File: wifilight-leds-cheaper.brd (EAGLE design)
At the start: 50.8 x 50.8 mm, 37 parts, among them Q1 BUK98180-100A, Q2 BUK98180-100A, Q3 BUK98180-100A, Q4 BUK98180-100A, U2 PCA9685

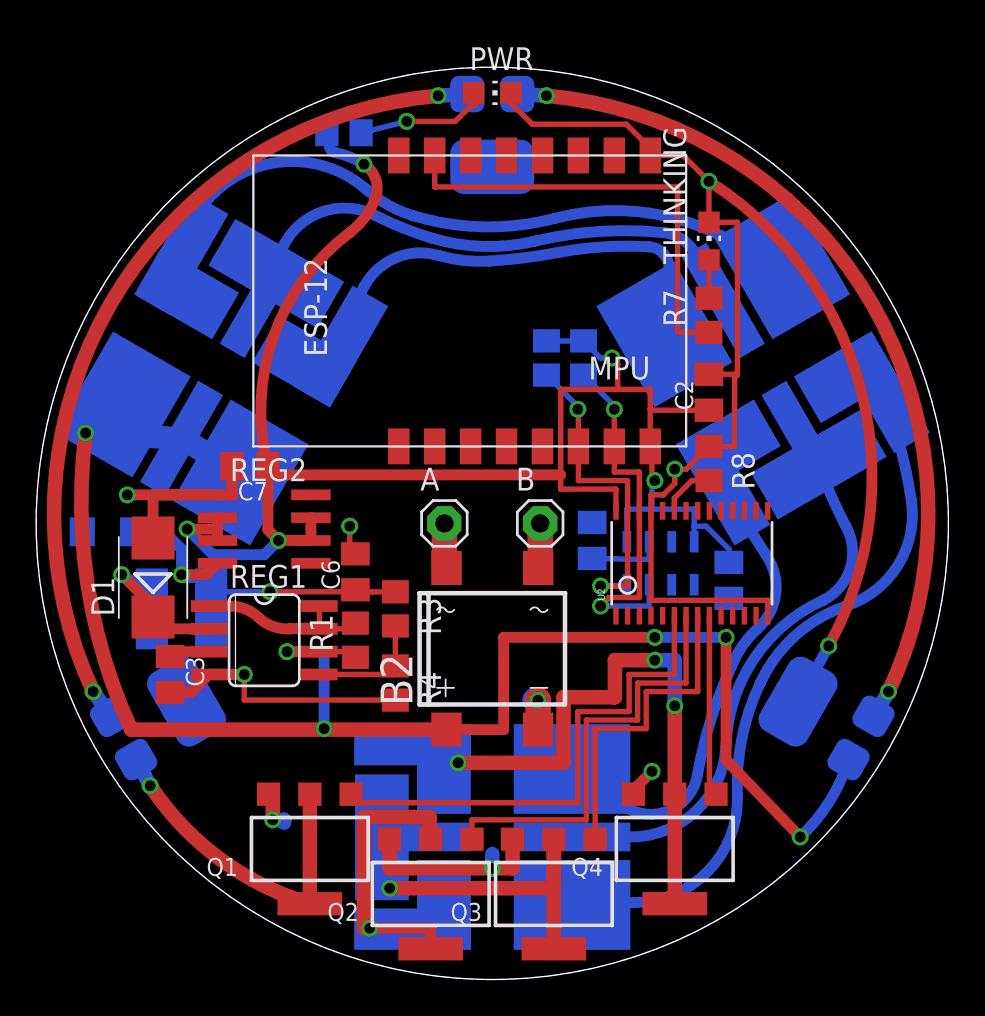
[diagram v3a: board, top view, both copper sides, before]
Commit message: Add a second ground plane on the top surface, pump it full of vias to help add thermal mass and heat spreading
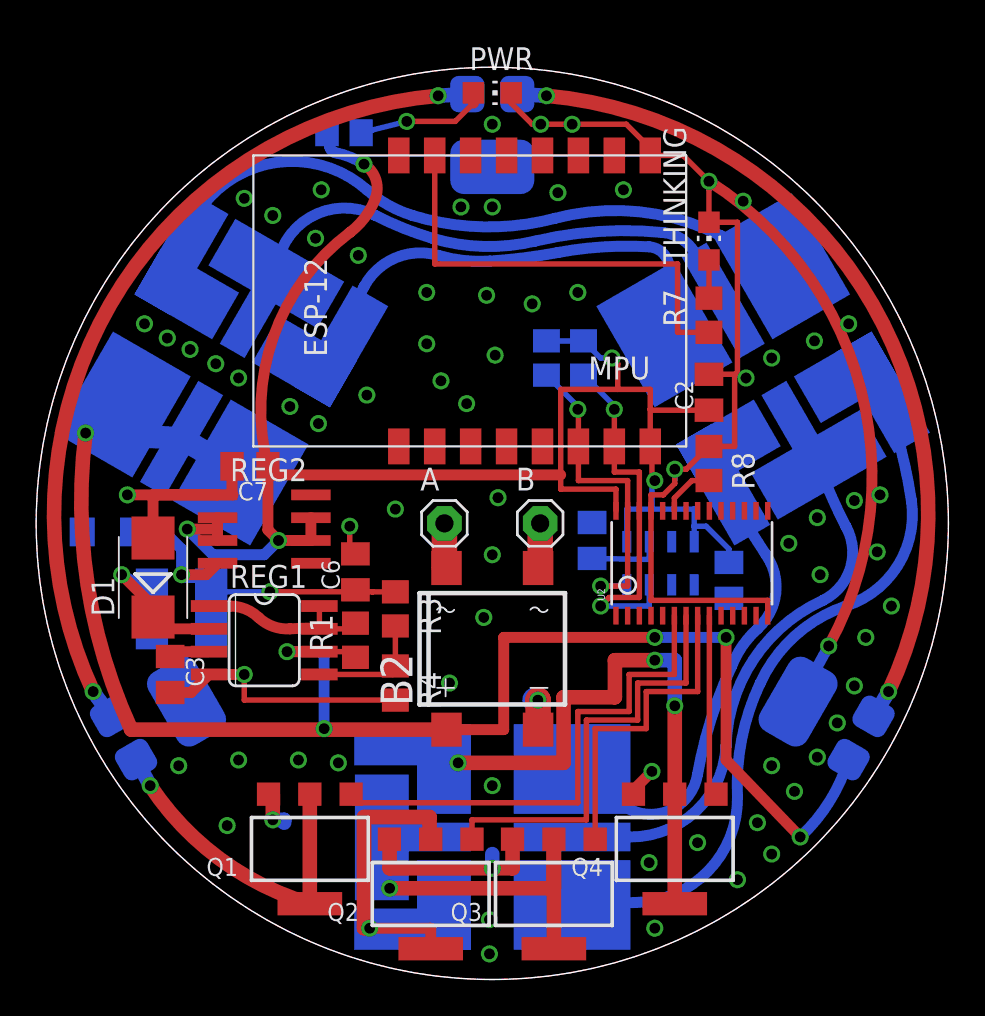
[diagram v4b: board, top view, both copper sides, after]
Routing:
- net GND: vias 10 -> 75
- added copper zone on layer 1, net GND
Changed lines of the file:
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@@
 <wire x1="26.45" y1="49.37125" x2="26.45" y2="48.7975" width="0.3048" layer="1"/>
 <wire x1="26.45" y1="48.7975" x2="27.6225" y2="47.625" width="0.3048" layer="1"/>
-<wire x1="27.6225" y1="47.625" x2="32.86125" y2="47.625" width="0.3048" layer="1"/>
+<wire x1="27.6225" y1="47.625" x2="28.09875" y2="47.625" width="0.3048" layer="1"/>
+<wire x1="28.09875" y1="47.625" x2="29.845" y2="47.625" width="0.3048" layer="1"/>
+<wire x1="29.845" y1="47.625" x2="32.86125" y2="47.625" width="0.3048" layer="1"/>
 <wire x1="32.86125" y1="47.625" x2="33.9725" y2="46.51375" width="0.3048" layer="1"/>
 <wire x1="33.9725" y1="46.51375" x2="33.9725" y2="46.10875" width="0.3048" layer="1"/>
@@
 <wire x1="34.29" y1="11.58875" x2="33.26" y2="10.55875" width="0.6096" layer="1"/>
 <wire x1="33.26" y1="10.55875" x2="33.26" y2="10.32075" width="0.6096" layer="1"/>
+<polygon width="0.6096" layer="1">
+<vertex x="25.4" y="50.8" curve="90"/>
+<vertex x="0" y="25.4" curve="90"/>
+<vertex x="25.4" y="0" curve="90"/>
+<vertex x="50.8" y="25.4" curve="90"/>
+</polygon>
+<via x="28.09875" y="47.625" extent="1-16" drill="0.6"/>
+<via x="29.845" y="47.625" extent="1-16" drill="0.6"/>
+<via x="17.93875" y="40.3225" extent="1-16" drill="0.6"/>
+<via x="21.74875" y="38.25875" extent="1-16" drill="0.6"/>
+<via x="21.74875" y="35.40125" extent="1-16" drill="0.6"/>
+<via x="22.5425" y="33.3375" extent="1-16" drill="0.6"/>
+<via x="23.97125" y="32.0675" extent="1-16" drill="0.6"/>
+<via x="25.55875" y="34.76625" extent="1-16" drill="0.6"/>
+<via x="25.0825" y="38.1" extent="1-16" drill="0.6"/>
+<via x="27.6225" y="37.62375" extent="1-16" drill="0.6"/>
+<via x="30.1625" y="38.25875" extent="1-16" drill="0.6"/>
+<via x="25.4" y="47.625" extent="1-16" drill="0.6"/>
+<via x="18.415" y="32.54375" extent="1-16" drill="0.6"/>
+<via x="7.9375" y="11.90625" extent="1-16" drill="0.6"/>
+<via x="11.27125" y="12.22375" extent="1-16" drill="0.6"/>
+<via x="10.63625" y="8.5725" extent="1-16" drill="0.6"/>
+<via x="14.605" y="12.22375" extent="1-16" drill="0.6"/>
+<via x="16.8275" y="12.065" extent="1-16" drill="0.6"/>
+<via x="25.24125" y="3.33375" extent="1-16" drill="0.6"/>
+<via x="25.24125" y="1.42875" extent="1-16" drill="0.6"/>
+<via x="42.2275" y="10.4775" extent="1-16" drill="0.6"/>
+<via x="40.9575" y="11.90625" extent="1-16" drill="0.6"/>
+<via x="43.4975" y="12.3825" extent="1-16" drill="0.6"/>
+<via x="44.60875" y="14.2875" extent="1-16" drill="0.6"/>
+<via x="45.56125" y="16.35125" extent="1-16" drill="0.6"/>
+<via x="46.19625" y="19.05" extent="1-16" drill="0.6"/>
+<via x="47.625" y="20.79625" extent="1-16" drill="0.6"/>
+<via x="43.65625" y="22.5425" extent="1-16" drill="0.6"/>
+<via x="43.4975" y="25.7175" extent="1-16" drill="0.6"/>
+<via x="41.91" y="24.28875" extent="1-16" drill="0.6"/>
+<via x="45.56125" y="26.67" extent="1-16" drill="0.6"/>
+<via x="46.99" y="26.9875" extent="1-16" drill="0.6"/>
+<via x="46.83125" y="23.8125" extent="1-16" drill="0.6"/>
+<via x="39.52875" y="33.49625" extent="1-16" drill="0.6"/>
+<via x="40.9575" y="34.6075" extent="1-16" drill="0.6"/>
+<via x="43.33875" y="35.56" extent="1-16" drill="0.6"/>
+<via x="45.24375" y="36.5125" extent="1-16" drill="0.6"/>
+<via x="15.71625" y="30.95625" extent="1-16" drill="0.6"/>
+<via x="11.27125" y="33.49625" extent="1-16" drill="0.6"/>
+<via x="10.00125" y="34.29" extent="1-16" drill="0.6"/>
+<via x="8.5725" y="35.08375" extent="1-16" drill="0.6"/>
+<via x="7.3025" y="35.71875" extent="1-16" drill="0.6"/>
+<via x="6.0325" y="36.5125" extent="1-16" drill="0.6"/>
+<via x="14.12875" y="31.90875" extent="1-16" drill="0.6"/>
+<via x="15.5575" y="41.275" extent="1-16" drill="0.6"/>
+<via x="13.17625" y="42.545" extent="1-16" drill="0.6"/>
+<via x="11.58875" y="43.4975" extent="1-16" drill="0.6"/>
+<via x="15.875" y="43.97375" extent="1-16" drill="0.6"/>
+<via x="39.37" y="43.33875" extent="1-16" drill="0.6"/>
+<via x="23.65375" y="43.02125" extent="1-16" drill="0.6"/>
+<via x="25.4" y="43.02125" extent="1-16" drill="0.6"/>
+<via x="29.05125" y="43.815" extent="1-16" drill="0.6"/>
+<via x="32.7025" y="43.97375" extent="1-16" drill="0.6"/>
+<via x="25.4" y="10.795" extent="1-16" drill="0.6"/>
+<via x="34.13125" y="6.50875" extent="1-16" drill="0.6"/>
+<via x="36.83" y="7.62" extent="1-16" drill="0.6"/>
+<via x="34.44875" y="2.8575" extent="1-16" drill="0.6"/>
+<via x="39.0525" y="5.55625" extent="1-16" drill="0.6"/>
+<via x="40.9575" y="6.985" extent="1-16" drill="0.6"/>
+<via x="40.16375" y="8.73125" extent="1-16" drill="0.6"/>
+<via x="20.0025" y="26.19375" extent="1-16" drill="0.6"/>
+<via x="25.7175" y="26.82875" extent="1-16" drill="0.6"/>
+<via x="25.4" y="23.65375" extent="1-16" drill="0.6"/>
+<via x="24.92375" y="20.16125" extent="1-16" drill="0.6"/>
+<via x="23.01875" y="16.51" extent="1-16" drill="0.6"/>
+<wire x1="20.0025" y1="15.56" x2="23.01875" y2="16.51" width="0" layer="19" extent="1-1"/>
 </signal>
 <signal name="SCL">
@@
 <contactref element="R7" pad="1"/>
 <contactref element="MPU" pad="7"/>
-<wire x1="22.195" y1="45.88625" x2="22.195" y2="44.1325" width="0.3048" layer="1"/>
-<wire x1="22.195" y1="44.1325" x2="35.71875" y2="44.1325" width="0.3048" layer="1"/>
-<wire x1="35.71875" y1="44.1325" x2="35.71875" y2="36.03875" width="0.3048" layer="1"/>
+<wire x1="22.195" y1="45.88625" x2="22.195" y2="39.84625" width="0.3048" layer="1"/>
+<wire x1="22.195" y1="39.84625" x2="35.71875" y2="39.84625" width="0.3048" layer="1"/>
+<wire x1="35.71875" y1="39.84625" x2="35.71875" y2="36.03875" width="0.3048" layer="1"/>
 <wire x1="35.71875" y1="36.03875" x2="37.465" y2="36.03875" width="0.3048" layer="1"/>
 </signal>

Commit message: Adding pogopin contacts
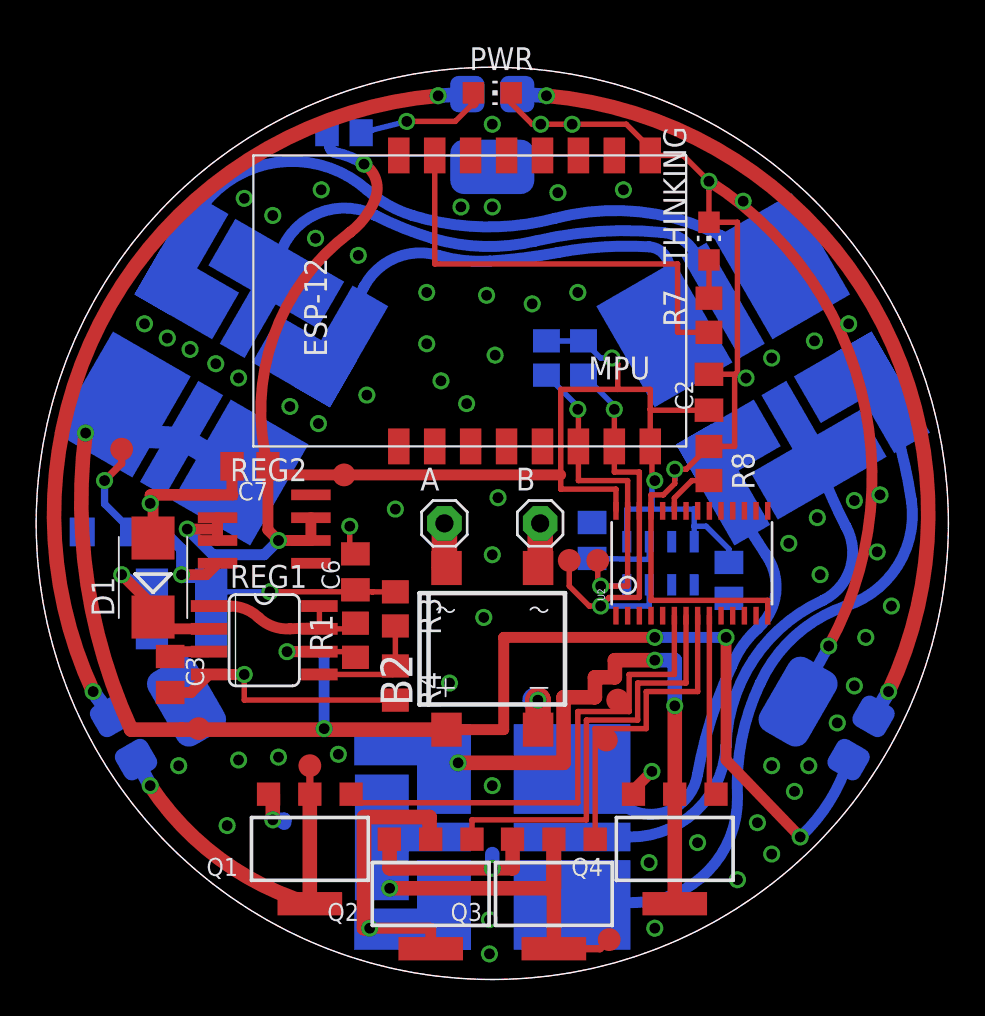
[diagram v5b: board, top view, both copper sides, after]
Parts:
- added P_RED, P_WHITE, RED, SCL, SDA, TP12V, TP3.3V, TP5V, WHITE: TEST-POINT3X5, SparkFun-Passives:PAD.03X.05
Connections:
- net 12V: now also TP12V.P$1
- net 3.3V: now also TP3.3V.P$1
- net 5V: now also TP5V.P$1
- net P_RED: now also P_RED.P$1
- net P_WHITE: now also P_WHITE.P$1
- net RED: now also RED.P$1
- net SCL: now also SCL.P$1
- net SDA: now also SDA.P$1
- net WHITE: now also WHITE.P$1
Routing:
- net 5V: track 20.5 -> 26.1 mm, vias 2 -> 3
- net SCL: track 20.7 -> 24.4 mm
- net P_RED: track 21.2 -> 24.5 mm
- net P_WHITE: track 18.8 -> 20.4 mm
- net SDA: track 18.3 -> 19.8 mm
- net 12V: track 110.6 -> 111.5 mm
- net WHITE: track 28.8 -> 29.7 mm
- net RED: track 18.2 -> 19.0 mm
- net GND: track 129.0 -> 128.2 mm
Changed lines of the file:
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@@
 <element name="Q1" library="nxp_60" package="SOT223" value="BUK98180-100A" x="15.24" y="7.27075" rot="R180"/>
 <element name="Q2" library="nxp_60" package="SOT223" value="BUK98180-100A" x="21.971" y="4.7625" rot="R180"/>
+<element name="TP12V" library="SparkFun-Passives" package="PAD.03X.05" value="TEST-POINT3X5" x="9.04875" y="13.97"/>
+<element name="TP5V" library="SparkFun-Passives" package="PAD.03X.05" value="TEST-POINT3X5" x="4.7625" y="29.5275"/>
+<element name="TP3.3V" library="SparkFun-Passives" package="PAD.03X.05" value="TEST-POINT3X5" x="17.145" y="28.09875"/>
+<element name="SCL" library="SparkFun-Passives" package="PAD.03X.05" value="TEST-POINT3X5" x="29.68625" y="23.33625"/>
+<element name="SDA" library="SparkFun-Passives" package="PAD.03X.05" value="TEST-POINT3X5" x="31.27375" y="23.33625"/>
+<element name="WHITE" library="SparkFun-Passives" package="PAD.03X.05" value="TEST-POINT3X5" x="32.385" y="15.5575"/>
+<element name="RED" library="SparkFun-Passives" package="PAD.03X.05" value="TEST-POINT3X5" x="31.75" y="13.335"/>
+<element name="P_WHITE" library="SparkFun-Passives" package="PAD.03X.05" value="TEST-POINT3X5" x="15.24" y="11.90625"/>
+<element name="P_RED" library="SparkFun-Passives" package="PAD.03X.05" value="TEST-POINT3X5" x="31.90875" y="2.2225"/>
 </elements>
 <signals>
@@
 <wire x1="11.58875" y1="15.56" x2="11.58875" y2="16.98625" width="0.3048" layer="1"/>
 <via x="11.58875" y="16.98625" extent="1-16" drill="0.6"/>
-<wire x1="10.1" y1="26.9875" x2="5.08" y2="26.9875" width="0.6096" layer="1"/>
-<via x="5.08" y="26.9875" extent="1-16" drill="0.6"/>
+<wire x1="10.1" y1="26.9875" x2="6.35" y2="26.9875" width="0.6096" layer="1"/>
+<wire x1="6.35" y1="26.9875" x2="6.35" y2="26.51125" width="0.6096" layer="1"/>
+<via x="6.35" y="26.51125" extent="1-16" drill="0.6"/>
 <wire x1="17.78" y1="23.70125" x2="17.4625" y2="23.70125" width="0.3048" layer="1"/>
 <wire x1="17.4625" y1="23.70125" x2="17.4625" y2="25.24125" width="0.3048" layer="1"/>
@@
 <via x="11.27125" y="12.22375" extent="1-16" drill="0.6"/>
 <via x="10.63625" y="8.5725" extent="1-16" drill="0.6"/>
-<via x="14.605" y="12.22375" extent="1-16" drill="0.6"/>
-<via x="16.8275" y="12.065" extent="1-16" drill="0.6"/>
+<via x="13.49375" y="12.3825" extent="1-16" drill="0.6"/>
+<via x="16.8275" y="12.54125" extent="1-16" drill="0.6"/>
 <via x="25.24125" y="3.33375" extent="1-16" drill="0.6"/>
 <via x="25.24125" y="1.42875" extent="1-16" drill="0.6"/>
 <via x="42.2275" y="10.4775" extent="1-16" drill="0.6"/>
 <via x="40.9575" y="11.90625" extent="1-16" drill="0.6"/>
-<via x="43.4975" y="12.3825" extent="1-16" drill="0.6"/>
+<via x="43.02125" y="11.90625" extent="1-16" drill="0.6"/>
 <via x="44.60875" y="14.2875" extent="1-16" drill="0.6"/>
 <via x="45.56125" y="16.35125" extent="1-16" drill="0.6"/>
@@
 <via x="24.92375" y="20.16125" extent="1-16" drill="0.6"/>
 <via x="23.01875" y="16.51" extent="1-16" drill="0.6"/>
-<wire x1="20.0025" y1="15.56" x2="23.01875" y2="16.51" width="0" layer="19" extent="1-1"/>
 </signal>
 <signal name="SCL">
@@
 <wire x1="32.195" y1="31.75" x2="32.195" y2="31.9425" width="0.3048" layer="16"/>
 <wire x1="32.195" y1="31.9425" x2="30.48" y2="33.6575" width="0.3048" layer="16"/>
+<contactref element="SCL" pad="P$1"/>
+<wire x1="29.68625" y1="23.33625" x2="29.68625" y2="21.9075" width="0.3048" layer="1"/>
+<wire x1="29.68625" y1="21.9075" x2="30.7975" y2="20.79625" width="0.3048" layer="1"/>
+<wire x1="30.7975" y1="20.79625" x2="31.4325" y2="20.79625" width="0.3048" layer="1"/>
 </signal>
 <signal name="SDA">
@@
 <wire x1="30.1625" y1="31.75" x2="30.1625" y2="31.91125" width="0.3048" layer="16"/>
 <wire x1="30.1625" y1="31.91125" x2="28.41625" y2="33.6575" width="0.3048" layer="16"/>
+<contactref element="SDA" pad="P$1"/>
+<wire x1="31.27375" y1="23.33625" x2="31.27375" y2="22.06625" width="0.3048" layer="1"/>
+<wire x1="31.27375" y1="22.06625" x2="31.4325" y2="21.9075" width="0.3048" layer="1"/>
 </signal>
 <signal name="GREEN">
@@
 <signal name="RED">
 <contactref element="Q3" pad="1"/>
-<wire x1="31.129" y1="7.8125" x2="31.129" y2="13.97" width="0.3048" layer="1"/>
+<wire x1="31.129" y1="7.8125" x2="31.129" y2="13.956" width="0.3048" layer="1"/>
 <wire x1="31.129" y1="13.97" x2="33.9725" y2="13.97" width="0.3048" layer="1"/>
 <wire x1="33.9725" y1="13.97" x2="33.9725" y2="16.03375" width="0.3048" layer="1"/>
@@
 <contactref element="U2" pad="8"/>
 <wire x1="36.8375" y1="20.2597" x2="36.8375" y2="16.03375" width="0.3048" layer="1"/>
+<contactref element="RED" pad="P$1"/>
+<wire x1="31.129" y1="13.97" x2="31.129" y2="13.956" width="0.3048" layer="1"/>
+<wire x1="31.129" y1="13.956" x2="31.75" y2="13.335" width="0.3048" layer="1"/>
 </signal>
 <signal name="BLUE">
@@
 <wire x1="33.02" y1="16.98625" x2="35.5375" y2="16.98625" width="0.3048" layer="1"/>
 <wire x1="35.5375" y1="20.2597" x2="35.5375" y2="16.98625" width="0.3048" layer="1"/>
+<contactref element="WHITE" pad="P$1"/>
+<wire x1="33.02" y1="14.9225" x2="32.385" y2="15.5575" width="0.3048" layer="1"/>
 </signal>
 <signal name="P_RED">
@@
 <wire x1="19.685" y1="5.08" x2="19.685" y2="7.9125" width="0.8128" layer="16"/>
 <wire x1="19.685" y1="7.9125" x2="19.25" y2="7.9125" width="0.8128" layer="16"/>
+<contactref element="P_RED" pad="P$1"/>
+<wire x1="28.829" y1="1.7125" x2="31.39875" y2="1.7125" width="0.4064" layer="1"/>
+<wire x1="31.39875" y1="1.7125" x2="31.90875" y2="2.2225" width="0.4064" layer="1"/>
 </signal>
 <signal name="P_WHITE">
@@
 <wire x1="6.35" y1="10.795" x2="15.24" y2="4.22075" width="0.8128" layer="1" curve="40"/>
 <wire x1="15.24" y1="10.32075" x2="15.24" y2="4.22075" width="0.8128" layer="1"/>
+<contactref element="P_WHITE" pad="P$1"/>
+<wire x1="15.24" y1="10.32075" x2="15.24" y2="11.90625" width="0.4064" layer="1"/>
 </signal>
 <signal name="P_BLUE">
@@
 <via x="34.44875" y="17.78" extent="1-16" drill="0.6"/>
 <wire x1="34.44875" y1="17.78" x2="32.22625" y2="17.78" width="0.8128" layer="1"/>
-<wire x1="32.22625" y1="17.78" x2="32.22625" y2="15.71625" width="0.8128" layer="1"/>
-<wire x1="32.22625" y1="15.71625" x2="29.36875" y2="15.71625" width="0.8128" layer="1"/>
+<wire x1="32.22625" y1="17.78" x2="32.22625" y2="16.8275" width="0.8128" layer="1"/>
+<wire x1="32.22625" y1="16.8275" x2="31.115" y2="16.8275" width="0.8128" layer="1"/>
+<wire x1="31.115" y1="16.8275" x2="31.115" y2="15.71625" width="0.8128" layer="1"/>
+<wire x1="31.115" y1="15.71625" x2="29.36875" y2="15.71625" width="0.8128" layer="1"/>
 <wire x1="29.36875" y1="15.71625" x2="29.36875" y2="12.065" width="0.8128" layer="1"/>
 <wire x1="29.36875" y1="12.065" x2="23.495" y2="12.065" width="0.8128" layer="1"/>
@@
 <wire x1="2.755028125" y1="30.430765625" x2="8.097553125" y2="30.125265625" width="1.27" layer="16"/>
 <wire x1="8.097553125" y1="30.125265625" x2="11.376325" y2="28.232265625" width="1.27" layer="16"/>
-<wire x1="22.85" y1="13.915" x2="5.295028125" y2="13.915" width="0.8128" layer="1"/>
+<wire x1="22.85" y1="13.915" x2="8.09625" y2="13.915" width="0.8128" layer="1"/>
+<wire x1="8.09625" y1="13.915" x2="5.295028125" y2="13.915" width="0.8128" layer="1"/>
 <wire x1="5.295028125" y1="13.915" x2="2.755028125" y2="30.430765625" width="0.8128" layer="1" curve="-32"/>
 <via x="2.755028125" y="30.430765625" extent="1-16" drill="0.6"/>
@@
 <via x="13.97" y="18.25625" extent="1-16" drill="0.6"/>
 <wire x1="13.97" y1="18.25625" x2="15.7734" y2="18.25625" width="0.6096" layer="1"/>
+<contactref element="TP12V" pad="P$1"/>
+<wire x1="9.04875" y1="13.97" x2="8.99375" y2="13.915" width="0.4064" layer="1"/>
+<wire x1="8.99375" y1="13.915" x2="8.09625" y2="13.915" width="0.4064" layer="1"/>
 </signal>
 <signal name="N$10">
@@
 <wire x1="32.0675" y1="34.6075" x2="31.43" y2="34.6075" width="0.3048" layer="16"/>
 <wire x1="31.43" y1="34.6075" x2="30.48" y2="35.5575" width="0.3048" layer="16"/>
-<wire x1="29.21" y1="28.09875" x2="12.90625" y2="28.09875" width="0.6096" layer="1"/>
+<wire x1="29.21" y1="28.09875" x2="17.145" y2="28.09875" width="0.6096" layer="1"/>
+<wire x1="17.145" y1="28.09875" x2="16.66875" y2="28.09875" width="0.6096" layer="1"/>
+<wire x1="16.66875" y1="28.09875" x2="12.90625" y2="28.09875" width="0.6096" layer="1"/>
 <wire x1="12.90625" y1="28.09875" x2="12.90625" y2="28.575" width="0.6096" layer="1"/>
 <wire x1="38.57625" y1="23.225" x2="38.57625" y2="23.97125" width="0.3048" layer="16"/>
@@
 <wire x1="18.89125" y1="43.4975" x2="17.4625" y2="41.5925" width="0.6096" layer="1" curve="-32.413213"/>
 <wire x1="17.4625" y1="41.5925" x2="12.90625" y2="28.575" width="0.6096" layer="1" curve="67.571913"/>
+<contactref element="TP3.3V" pad="P$1"/>
 </signal>
 <signal name="N$13">
@@
 <wire x1="18.7325" y1="21.5875" x2="17.78" y2="21.5875" width="0.3048" layer="1"/>
 <wire x1="17.78" y1="21.5875" x2="17.78" y2="21.70125" width="0.3048" layer="1"/>
+<contactref element="TP5V" pad="P$1"/>
+<via x="3.81" y="27.78125" extent="1-16" drill="0.6"/>
+<wire x1="3.81" y1="27.78125" x2="4.7625" y2="28.73375" width="0.4064" layer="1"/>
+<wire x1="4.7625" y1="28.73375" x2="4.7625" y2="29.5275" width="0.4064" layer="1"/>
+<wire x1="5.36875" y1="24.92375" x2="3.81" y2="26.4825" width="0.4064" layer="16"/>
+<wire x1="3.81" y1="26.4825" x2="3.81" y2="27.78125" width="0.4064" layer="16"/>
 </signal>
 <signal name="COMP">
